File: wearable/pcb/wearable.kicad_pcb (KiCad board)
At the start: 4 copper layers, 28 x 39.2 mm, 83 parts, among them J1 USB_C_Receptacle_USB2.0, J2 Extension, J3 Extension, U1 BC833, U10 TCR3UFxxA, U11 TMP1075, U2 MCP73832-2-OT, U3 S-85S1A, U4 LIS2DE12, U5 APDS-9250, U6 MX25R8035FZxxx0, U7 PCF85063ATL, U8 DT1446-04V, U9 MAX30102, Y71 32.768kHz

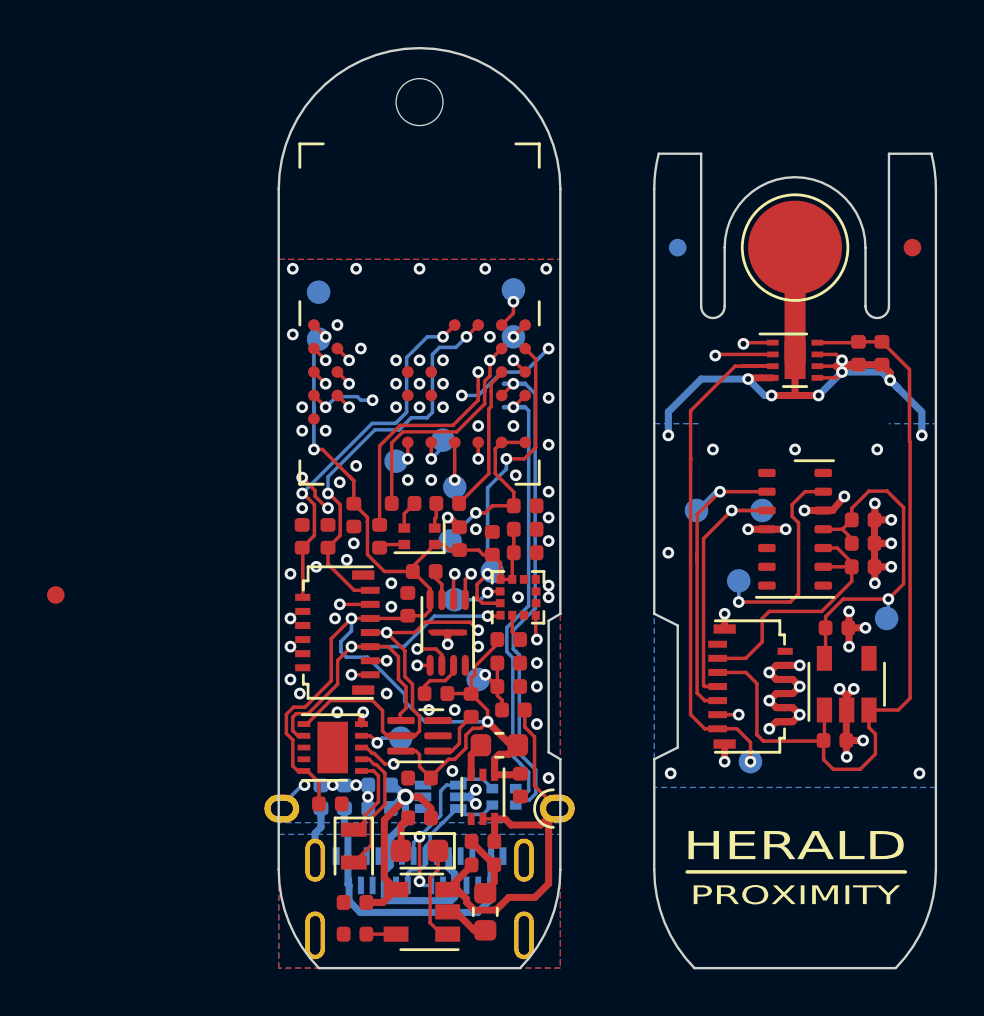
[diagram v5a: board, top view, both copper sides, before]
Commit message: Nordic review: drop current limiting resitors from the USB.
Per @msromero: For D+ and D- lines it's recommend to get rid of the
22R resistors in parallel of the TVS diodes, since you can risk
failing USB testing.

Thanks!

Signed-off-by: Mike M. Volokhov <mike.volokhov@gmail.com>
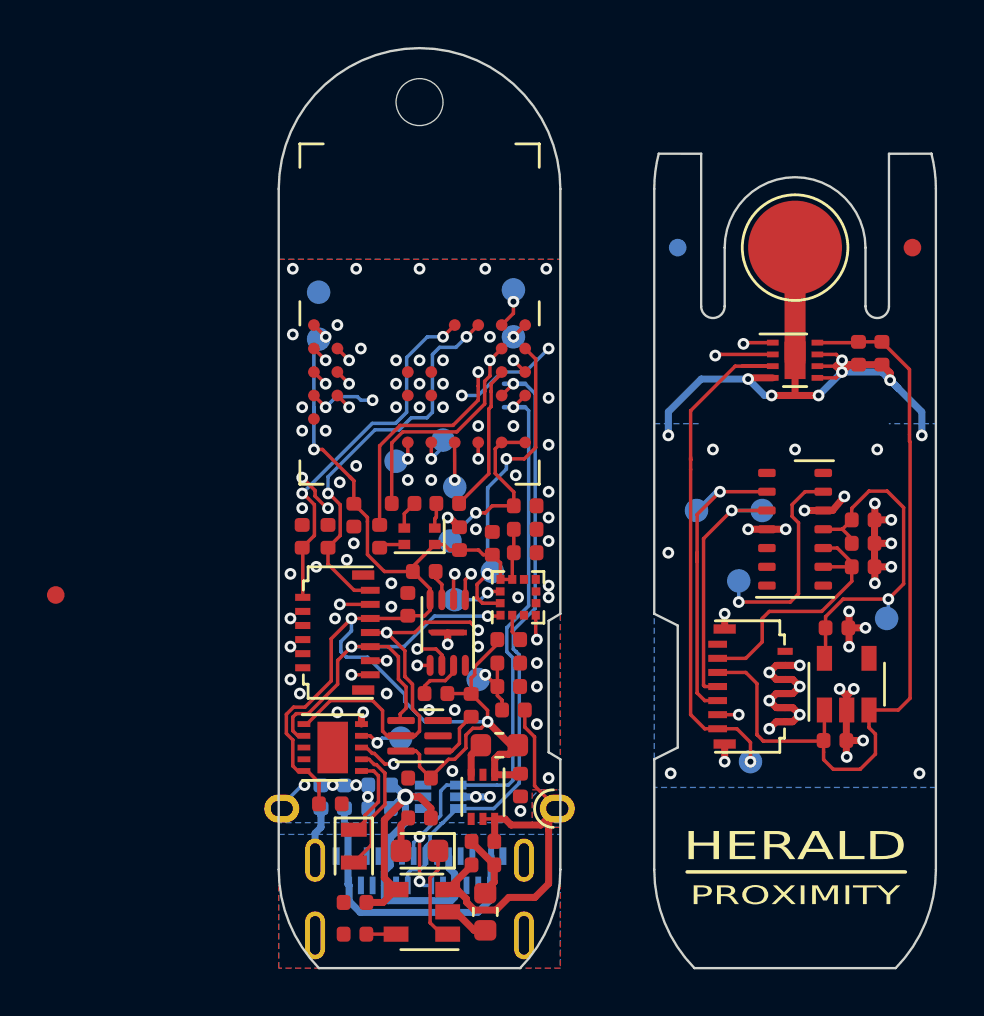
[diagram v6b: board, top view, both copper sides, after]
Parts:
- removed RN1: 22R, Resistor_SMD:R_Array_Convex_2x0402
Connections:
- J1 pad A6: Net-(J1-PadA6) -> /Core Board/USB_D+
- J1 pad A7: Net-(J1-PadA7) -> /Core Board/USB_D-
- J1 pad B6: Net-(J1-PadA6) -> /Core Board/USB_D+
- J1 pad B7: Net-(J1-PadA7) -> /Core Board/USB_D-
- U8 pad 1: Net-(J1-PadA7) -> /Core Board/USB_D-
- U8 pad 3: Net-(J1-PadA6) -> /Core Board/USB_D+
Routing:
- net Net-(J1-PadA7): track 8.30 -> 0.00 mm, vias 2 -> 0
- net /Core Board/USB_D-: track 19.5 -> 27.0 mm, vias 1 -> 3
- net /Core Board/USB_D+: track 21.1 -> 27.4 mm
- net Net-(J1-PadA6): track 6.15 -> 0.00 mm
- net GND: track 17.2 -> 17.3 mm, vias 73 -> 74
- added copper zone on B.Cu, net +BATT
- added copper zone on F.Cu, net +BATT
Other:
- board text added: "+"

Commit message: Tune the LED resistors.
The RGB LED resistors were tuned on a real board with 2.5V driver
voltage.  It happens the blue LED should be zero Ohm limited, and
then red and green LEDs adjusted to the neutral white.

The charge LED looks good with 5.1k, but more standard 5.6k should
also work just fine.

Signed-off-by: Mike M. Volokhov <mike.volokhov@gmail.com>
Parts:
- R1: value Tune -> 0
- R2: value Tune -> 3.9k
- R22: value Tune -> 5.6k
- R3: value Tune -> 1k
- R4: value 0 Ohm -> 0
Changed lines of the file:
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@@
       (effects (font (size 1 1) (thickness 0.15)))
     )
-    (fp_text value Tune (at 0 -0.6) (layer F.Fab)
+    (fp_text value 5.6k (at 0 -0.6) (layer F.Fab)
       (effects (font (size 0.4 0.4) (thickness 0.06)))
     )
@@
       (effects (font (size 1 1) (thickness 0.15)))
     )
-    (fp_text value Tune (at 0 -0.6) (layer F.Fab)
+    (fp_text value 1k (at 0 -0.6) (layer F.Fab)
       (effects (font (size 0.4 0.4) (thickness 0.06)))
     )
@@
       (effects (font (size 1 1) (thickness 0.15)))
     )
-    (fp_text value Tune (at -1.3 0 90) (layer F.Fab)
+    (fp_text value 3.9k (at -1.3 0 90) (layer F.Fab)
       (effects (font (size 0.4 0.4) (thickness 0.06)))
     )
@@
       (effects (font (size 1 1) (thickness 0.15)))
     )
-    (fp_text value Tune (at 0 0.6) (layer F.Fab)
+    (fp_text value 0 (at 0 0.6) (layer F.Fab)
       (effects (font (size 0.4 0.4) (thickness 0.06)))
     )
@@
       (effects (font (size 1 1) (thickness 0.15)))
     )
-    (fp_text value "0 Ohm" (at 0 0.8 90) (layer F.Fab)
-      (effects (font (size 0.4 0.4) (thickness 0.06)))
-    )
+    (fp_text value 0 (at 0 0.8 90) (layer F.Fab)
+      (effects (font (size 0.4 0.4) (thickness 0.06)))
+    )

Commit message: Tune the NFC antenna.
The antenna design is in the wearable/fpc directory.
S11: https://twitter.com/mishkathebear/status/1417551022650691590/photo/1

Signed-off-by: Mike M. Volokhov <mike.volokhov@gmail.com>
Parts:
- C13, C14: value Tune -> 390pF
